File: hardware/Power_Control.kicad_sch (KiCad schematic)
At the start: 15 parts, among them Q1 DMN65D8L, Q2 DMP2240UDM

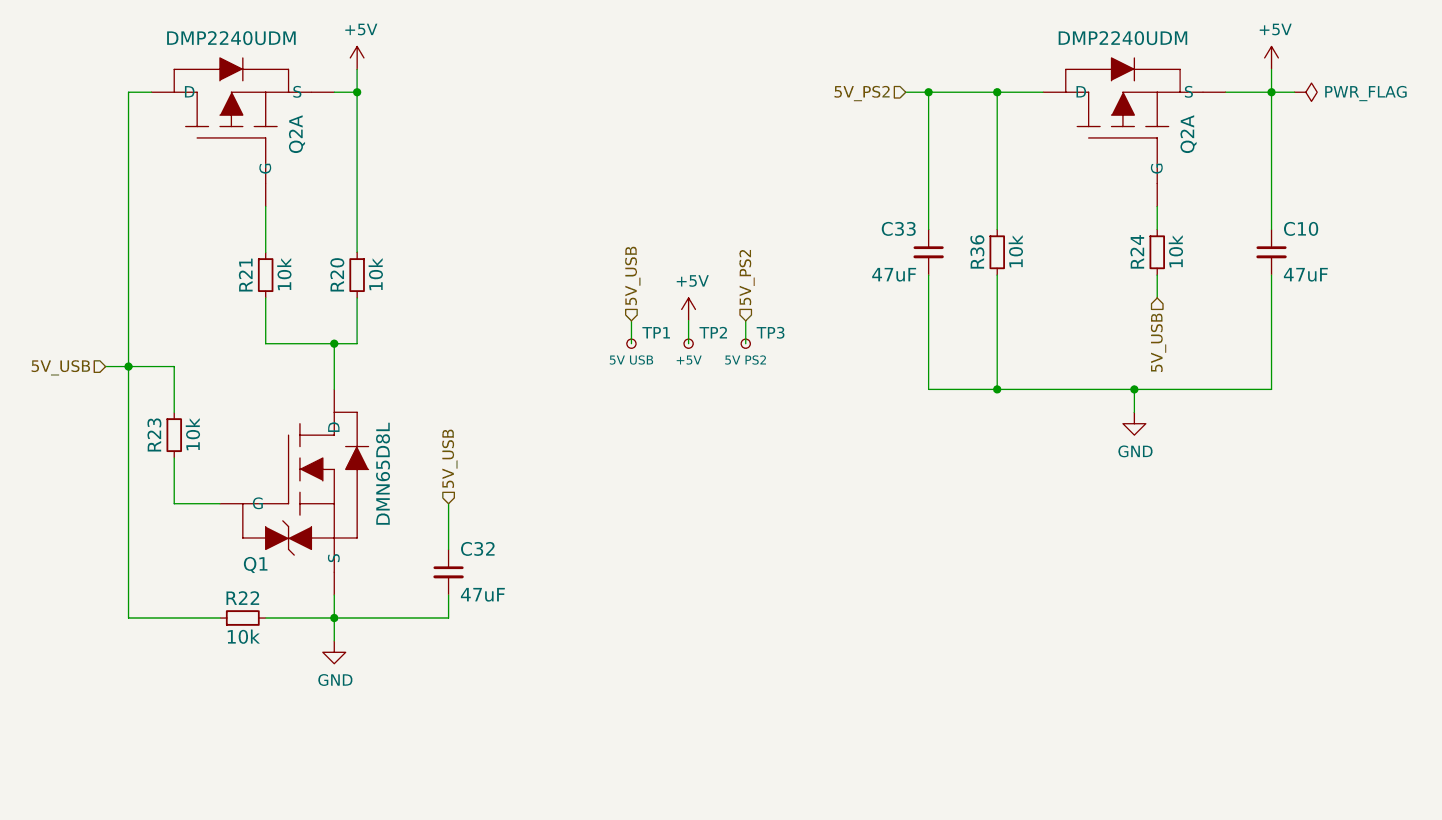
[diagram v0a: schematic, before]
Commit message: Improved a pile of the schematic, converting it to use KiCad schematic symbols and footprints instead of eagle imports
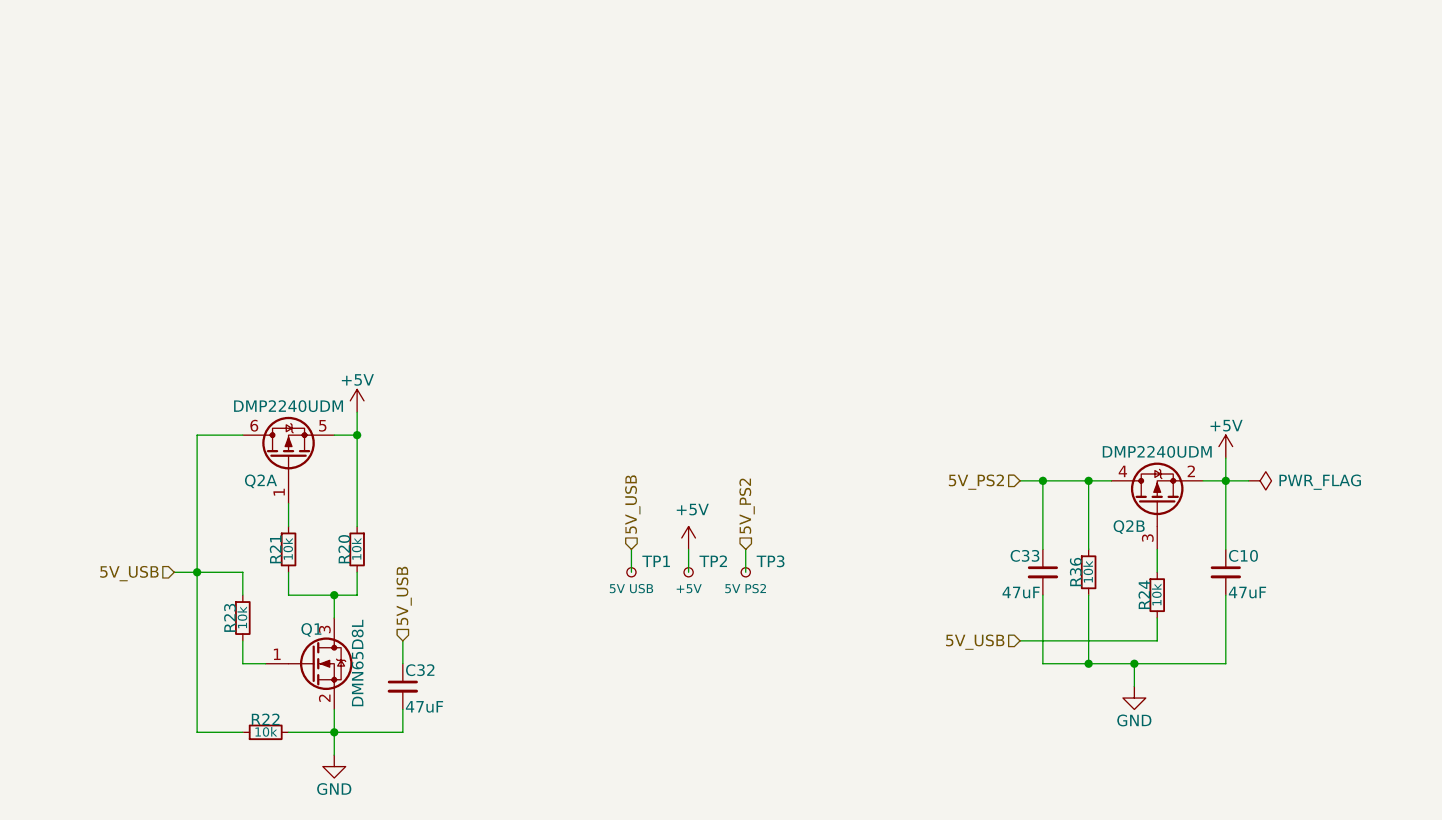
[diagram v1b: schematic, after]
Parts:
- Q1: symbol MXKeyboard-eagle-import:DMN65D8L -> Device:Q_NMOS_GSD
- Q2: symbol MXKeyboard-eagle-import:DMP2240UDM -> Device:Q_Dual_PMOS_G1S2G2D2S1D1
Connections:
- net +5V: now also Q2.2 (S); no longer Q2.5 (S)
- net 5V_PS2: now also Q2.4 (D); no longer Q2.6 (D)
- net at R24.1: now also Q2.3 (G); no longer Q2.1 (G)
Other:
- moved on the sheet: C10, C32, C33, R20, R21, R22, R23, R24, R36, TP1, TP2, TP3
